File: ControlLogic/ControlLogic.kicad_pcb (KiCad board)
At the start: 2 copper layers, 85 x 99.5 mm, 19 parts

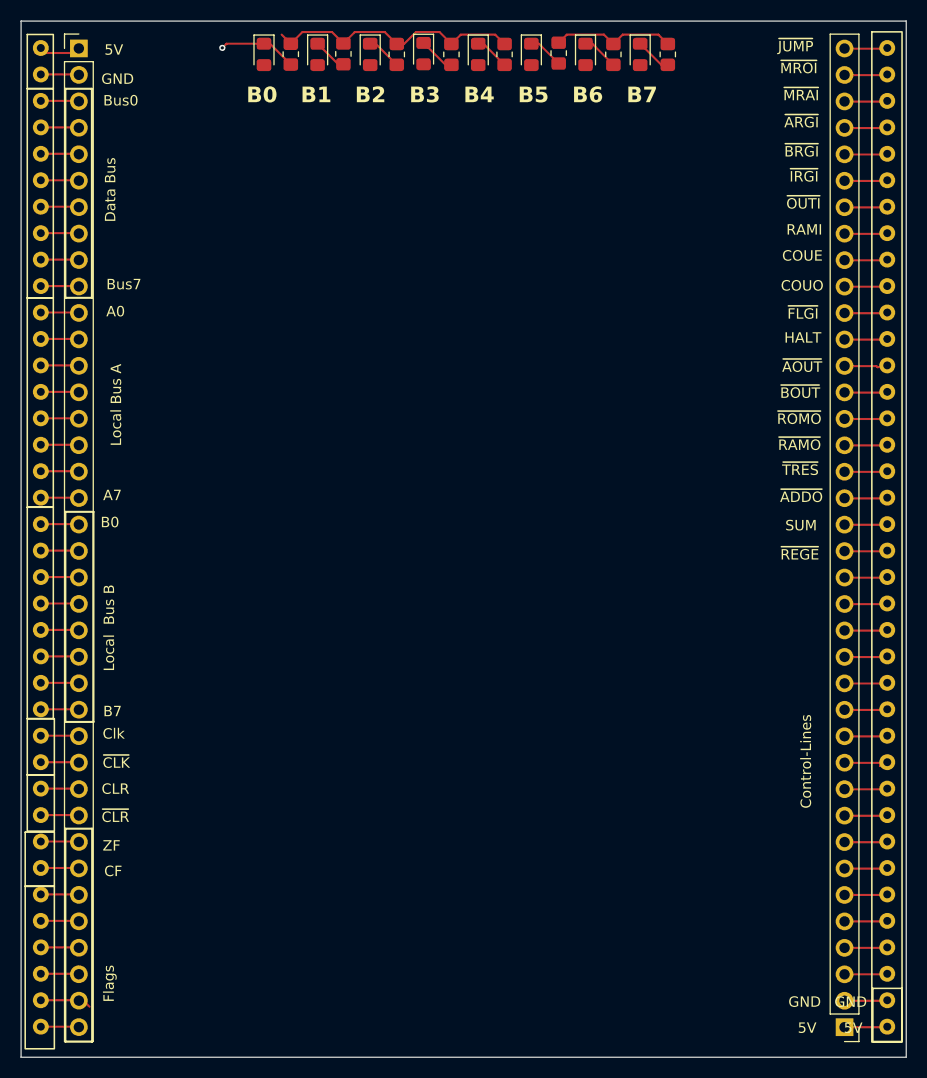
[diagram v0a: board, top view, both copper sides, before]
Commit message: [ControlLogic] - Routed and checked Control Logic board.
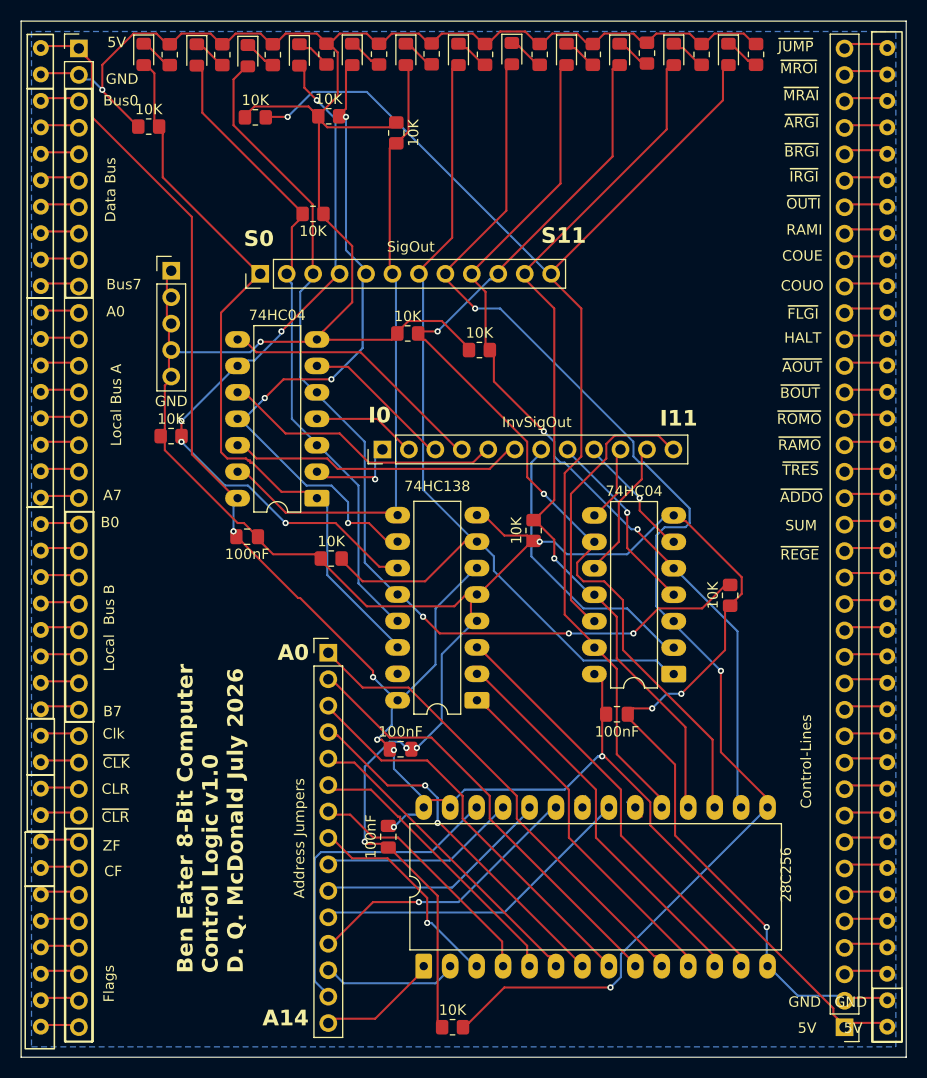
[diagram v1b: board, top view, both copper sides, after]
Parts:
- added C1: 100nF, Capacitor_SMD:C_0805_2012Metric_Pad1.18x1.45mm_HandSolder, F.Cu at (59.0, 107.0)
- added C2: 100nF, Capacitor_SMD:C_0805_2012Metric_Pad1.18x1.45mm_HandSolder, F.Cu at (60.2, 98.6)
- added C3: 100nF, Capacitor_SMD:C_0805_2012Metric_Pad1.18x1.45mm_HandSolder, F.Cu at (45.4, 78.2)
- added C4: 100nF, Capacitor_SMD:C_0805_2012Metric_Pad1.18x1.45mm_HandSolder, F.Cu at (80.9, 95.2)
- added D10: LED, LED_SMD:LED_0805_2012Metric_Pad1.15x1.40mm_HandSolder, F.Cu at (45.5, 32.0)
- added D11: LED, LED_SMD:LED_0805_2012Metric_Pad1.15x1.40mm_HandSolder, F.Cu at (40.6, 31.9)
- added D12: LED, LED_SMD:LED_0805_2012Metric_Pad1.15x1.40mm_HandSolder, F.Cu at (35.5, 31.9)
- added D9: LED, LED_SMD:LED_0805_2012Metric_Pad1.15x1.40mm_HandSolder, F.Cu at (50.5, 31.9)
- added J1: Address Jumpers, Connector_PinHeader_2.54mm:PinHeader_1x15_P2.54mm_Vertical, F.Cu at (53.2, 89.3)
- added J2: GND, Connector_PinHeader_2.54mm:PinHeader_1x05_P2.54mm_Vertical, F.Cu at (38.1, 52.6)
- added J3: SigOut, Connector_PinHeader_2.54mm:PinHeader_1x12_P2.54mm_Vertical, F.Cu at (46.7, 52.9)
- added J4: InvSigOut, Connector_PinHeader_2.54mm:PinHeader_1x12_P2.54mm_Vertical, F.Cu at (58.4, 69.8)
- added R10: 330R, Resistor_SMD:R_0805_2012Metric_Pad1.20x1.40mm_HandSolder, F.Cu at (47.9, 31.9)
- added R11: 330R, Resistor_SMD:R_0805_2012Metric_Pad1.20x1.40mm_HandSolder, F.Cu at (43.0, 31.9)
- added R12: 330R, Resistor_SMD:R_0805_2012Metric_Pad1.20x1.40mm_HandSolder, F.Cu at (38.0, 31.9)
- added R13: 10K, Resistor_SMD:R_0805_2012Metric_Pad1.20x1.40mm_HandSolder, F.Cu at (36.0, 38.8)
- added R14: 10K, Resistor_SMD:R_0805_2012Metric_Pad1.20x1.40mm_HandSolder, F.Cu at (51.8, 47.2)
- added R15: 10K, Resistor_SMD:R_0805_2012Metric_Pad1.20x1.40mm_HandSolder, F.Cu at (91.8, 83.8)
- added R16: 10K, Resistor_SMD:R_0805_2012Metric_Pad1.20x1.40mm_HandSolder, F.Cu at (38.1, 68.5)
- added R17: 10K, Resistor_SMD:R_0805_2012Metric_Pad1.20x1.40mm_HandSolder, F.Cu at (53.3, 37.8)
- added R18: 10K, Resistor_SMD:R_0805_2012Metric_Pad1.20x1.40mm_HandSolder, F.Cu at (59.8, 39.4)
- added R19: 10K, Resistor_SMD:R_0805_2012Metric_Pad1.20x1.40mm_HandSolder, F.Cu at (53.5, 80.3)
- added R20: 10K, Resistor_SMD:R_0805_2012Metric_Pad1.20x1.40mm_HandSolder, F.Cu at (65.2, 125.3)
- added R21: 10K, Resistor_SMD:R_0805_2012Metric_Pad1.20x1.40mm_HandSolder, F.Cu at (67.7, 60.3)
- added R22: 10K, Resistor_SMD:R_0805_2012Metric_Pad1.20x1.40mm_HandSolder, F.Cu at (60.9, 58.7)
- added R23: 10K, Resistor_SMD:R_0805_2012Metric_Pad1.20x1.40mm_HandSolder, F.Cu at (72.9, 77.6)
- added R24: 10K, Resistor_SMD:R_0805_2012Metric_Pad1.20x1.40mm_HandSolder, F.Cu at (46.2, 37.9)
- added R9: 330R, Resistor_SMD:R_0805_2012Metric_Pad1.20x1.40mm_HandSolder, F.Cu at (53.0, 31.9)
- added U1: 28C256, Package_DIP:DIP-28_W15.24mm_LongPads, F.Cu at (62.4, 119.4)
- added U2: 74HC138, Package_DIP:DIP-16_W7.62mm_LongPads, F.Cu at (67.5, 93.9)
- added U3: 74HC04, Package_DIP:DIP-14_W7.62mm_LongPads, F.Cu at (52.1, 74.5)
- added U4: 74HC04, Package_DIP:DIP-14_W7.62mm_LongPads, F.Cu at (86.4, 91.4)
- moved D3 8.47 mm to (81.2, 31.9)
- moved R3 8.47 mm to (83.8, 31.8)
- moved D5 8.47 mm to (70.9, 31.8)
- moved D6 8.47 mm to (65.7, 31.9)
- moved R7 8.47 mm to (63.2, 31.8)
- moved R8 8.47 mm to (58.1, 31.9)
- moved D1 8.47 mm to (91.6, 31.9)
- moved D2 8.47 mm to (86.4, 31.9)
- moved D4 8.47 mm to (76.1, 31.9)
- moved D7 8.47 mm to (60.7, 31.9)
- moved D8 8.47 mm to (55.5, 31.9)
- moved R1 8.47 mm to (94.3, 31.9)
- moved R2 8.47 mm to (89.1, 31.9)
- moved R4 8.47 mm to (78.6, 31.9)
- moved R5 8.47 mm to (73.5, 31.9)
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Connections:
- D1 pad 2: unconnected-(D1-A-Pad2) -> EPOUT11
- D2 pad 2: unconnected-(D2-A-Pad2) -> EPOUT10
- D3 pad 2: unconnected-(D3-A-Pad2) -> EPOUT9
- D4 pad 2: unconnected-(D4-A-Pad2) -> EPOUT8
- D5 pad 2: unconnected-(D5-A-Pad2) -> EPOUT7
- D6 pad 2: unconnected-(D6-A-Pad2) -> EPOUT6
- D7 pad 2: unconnected-(D7-A-Pad2) -> EPOUT5
- D8 pad 2: unconnected-(D8-A-Pad2) -> EPOUT4
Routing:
- net GND: track 45.3 -> 375.0 mm, vias 0 -> 9
- net 5V: track 9.15 -> 181.2 mm, vias 0 -> 6
- net EPOUT7: track 0.00 -> 131.4 mm, vias 0 -> 3
- net EPOUT11: track 0.00 -> 119.5 mm, vias 0 -> 1
- net EPOUT9: track 0.00 -> 94.8 mm, vias 0 -> 2
- net EPOUT2: track 0.00 -> 94.1 mm, vias 0 -> 3
- net EPOUT6: track 0.00 -> 90.1 mm
- net EPOUT8: track 0.00 -> 86.1 mm, vias 0 -> 2
- net EPOUT10: track 0.00 -> 85.5 mm, vias 0 -> 1
- net EPOUT0: track 0.00 -> 72.1 mm
- net EPOUT3: track 0.00 -> 70.3 mm, vias 0 -> 5
- net EPOUT4: track 0.00 -> 65.2 mm, vias 0 -> 4
- net EPOUT1: track 0.00 -> 62.5 mm
- net EPOUT5: track 0.00 -> 61.2 mm
- net ADD0: track 0.00 -> 46.0 mm
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- added copper zone on B.Cu, net GND
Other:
- board text added: "A0"
- board text added: "A14"
- board text added: "Ben Eater 8-Bit Computer Control Logic v1.0 D. Q. McDonald July 2026"
- board text added: "I0"
- board text added: "I11"
- board text added: "S0"
- board text added: "S11"
- board text removed: "B0"
- board text removed: "B1"
- board text removed: "B2"
- board text removed: "B3"
- board text removed: "B4"
- board text removed: "B5"
- board text removed: "B6"
- board text removed: "B7"

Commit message: [ControlLogic] - added second sets flags for Zero and Carry in case there's a second logic unit at some point.
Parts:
- added C5: 100nF, Capacitor_SMD:C_0805_2012Metric_Pad1.18x1.45mm_HandSolder, F.Cu at (45.9, 96.2)
- added J5: Flags, Connector_PinHeader_2.54mm:PinHeader_1x02_P2.54mm_Vertical, F.Cu at (41.3, 89.5)
- added R25: 10K, Resistor_SMD:R_0805_2012Metric_Pad1.20x1.40mm_HandSolder, F.Cu at (36.5, 96.8)
- added R26: 10K, Resistor_SMD:R_0805_2012Metric_Pad1.20x1.40mm_HandSolder, F.Cu at (35.6, 121.0)
- added R27: 10K, Resistor_SMD:R_0805_2012Metric_Pad1.20x1.40mm_HandSolder, F.Cu at (45.6, 121.2)
- added R28: 10K, Resistor_SMD:R_0805_2012Metric_Pad1.20x1.40mm_HandSolder, F.Cu at (40.6, 121.2)
- added U5: 74HC32, Package_DIP:DIP-14_W7.62mm_LongPads, F.Cu at (37.4, 100.2)
- J1: value Address Jumpers -> AddJumpers
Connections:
- net FL-2 renamed ZFLAG2
- net FL-3 renamed CFLAG2
- net ZFLG renamed ZFLAG
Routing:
- net ZFLAG: track 3.71 -> 38.2 mm, vias 0 -> 1
- net GND: track 375.0 -> 402.7 mm, vias 9 -> 10
- net CFLAG: track 3.68 -> 26.5 mm, vias 0 -> 1
- net CF: track 0.00 -> 22.5 mm
- net 5V: track 181.2 -> 201.9 mm
- net ZFLAG2: track 3.76 -> 23.9 mm
- net CFLAG2: track 3.72 -> 22.2 mm
- net ZF: track 0.00 -> 17.4 mm
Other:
- board text added: "Carry"
- board text added: "Zero"
